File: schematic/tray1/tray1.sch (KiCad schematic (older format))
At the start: 15 parts, among them J1 Conn_02x10_Odd_Even, J2 Conn_02x05_Odd_Even, J3 Conn_Coaxial, U1 ATmega128-16AU, U2 GPS, U3 ST485EBDR, U4 74HC04, Y1 TXCO

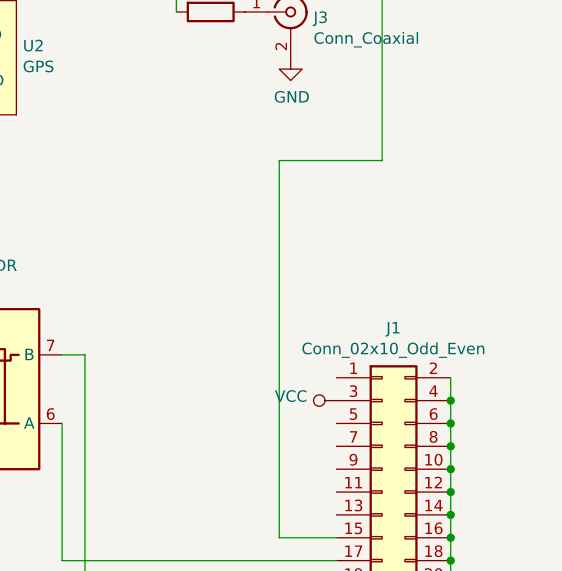
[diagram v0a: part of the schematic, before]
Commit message: Add separate regulator for low noise
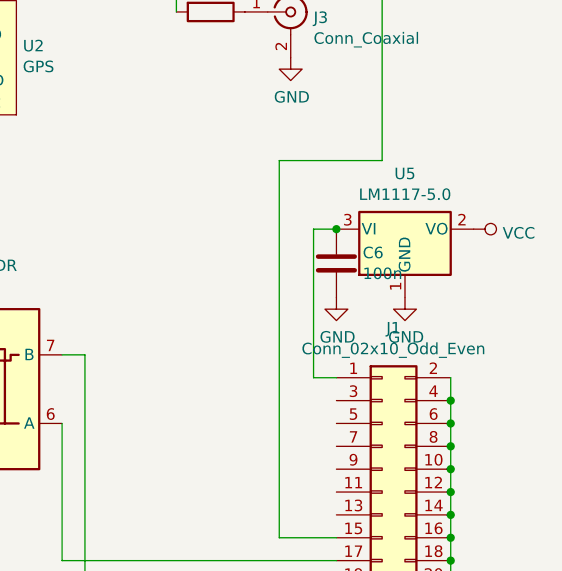
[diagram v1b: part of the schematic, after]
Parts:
- added C6: 100n, Capacitor_SMD:C_0805_2012Metric_Pad1.15x1.40mm_HandSolder, symbol Device:C
- added U5: LM1117-5.0, Package_TO_SOT_SMD:SOT-223-3_TabPin2, symbol Regulator_Linear:LM1117-5.0
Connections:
- net GND: now also C6.2, U5.1 (GND)
- net VCC: now also U5.2 (VO); no longer J1.3 (Pin_3)
- net at J1.1 (Pin_1): now also C6.1, U5.3 (VI)
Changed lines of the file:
@@
 L power:VCC #PWR015
 U 1 1 5DF5E04D
-P 8150 3900
-F 0 "#PWR015" H 8150 3750 50  0001 C CNN
-F 1 "VCC" V 8168 4027 50  0000 L CNN
-F 2 "" H 8150 3900 50  0001 C CNN
-F 3 "" H 8150 3900 50  0001 C CNN
-	1    8150 3900
-	0    -1   -1   0
+P 8750 3150
+F 0 "#PWR015" H 8750 3000 50  0001 C CNN
+F 1 "VCC" V 8768 3277 50  0000 L CNN
+F 2 "" H 8750 3150 50  0001 C CNN
+F 3 "" H 8750 3150 50  0001 C CNN
+	1    8750 3150
+	0    1    1    0
 $EndComp
 $Comp
@@
 	7900 4500 8150 4500
 Connection ~ 8300 1800
+$Comp
+L Regulator_Linear:LM1117-5.0 U5
+U 1 1 5E98CFED
+P 8450 3150
+F 0 "U5" H 8450 3392 50  0000 C CNN
+F 1 "LM1117-5.0" H 8450 3301 50  0000 C CNN
+F 2 "Package_TO_SOT_SMD:SOT-223-3_TabPin2" H 8450 3150 50  0001 C CNN
+F 3 "http://www.ti.com/lit/ds/symlink/lm1117.pdf" H 8450 3150 50  0001 C CNN
+	1    8450 3150
+	1    0    0    -1
+$EndComp
+$Comp
+L power:GND #PWR0103
+U 1 1 5E98E150
+P 8450 3450
+F 0 "#PWR0103" H 8450 3200 50  0001 C CNN
+F 1 "GND" H 8455 3277 50  0000 C CNN
+F 2 "" H 8450 3450 50  0001 C CNN
+F 3 "" H 8450 3450 50  0001 C CNN
+	1    8450 3450
+	1    0    0    -1
+$EndComp
+$Comp
+L Device:C C6
+U 1 1 5E98E7D3
+P 8150 3300
+F 0 "C6" H 8265 3346 50  0000 L CNN
+F 1 "100n" H 8265 3255 50  0000 L CNN
+F 2 "Capacitor_SMD:C_0805_2012Metric_Pad1.15x1.40mm_HandSolder" H 8188 3150 50  0001 C CNN
+F 3 "~" H 8150 3300 50  0001 C CNN
+	1    8150 3300
+	1    0    0    -1
+$EndComp
+$Comp
+L power:GND #PWR0104
+U 1 1 5E98F854
+P 8150 3450
+F 0 "#PWR0104" H 8150 3200 50  0001 C CNN
+F 1 "GND" H 8155 3277 50  0000 C CNN
+F 2 "" H 8150 3450 50  0001 C CNN
+F 3 "" H 8150 3450 50  0001 C CNN
+	1    8150 3450
+	1    0    0    -1
+$EndComp
+Wire Wire Line
+	8150 3150 8050 3150
+Wire Wire Line
+	8050 3150 8050 3800
+Wire Wire Line
+	8050 3800 8150 3800
+Connection ~ 8150 3150
 $EndSCHEMATC
